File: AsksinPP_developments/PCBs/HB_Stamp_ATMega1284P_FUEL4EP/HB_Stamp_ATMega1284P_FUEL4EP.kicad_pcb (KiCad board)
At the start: 2 copper layers, 22 x 40 mm, 39 parts, among them J1 Power, J2 FTDI Debuger, J3 ISP Programmer, J4 I2C, J5 PA5/PCINT5, J6 PB3/AIN1/PCINT11, J7 PC4/PCINT20, U1 ATmega1284P-AU, U2 TPS61221DCK

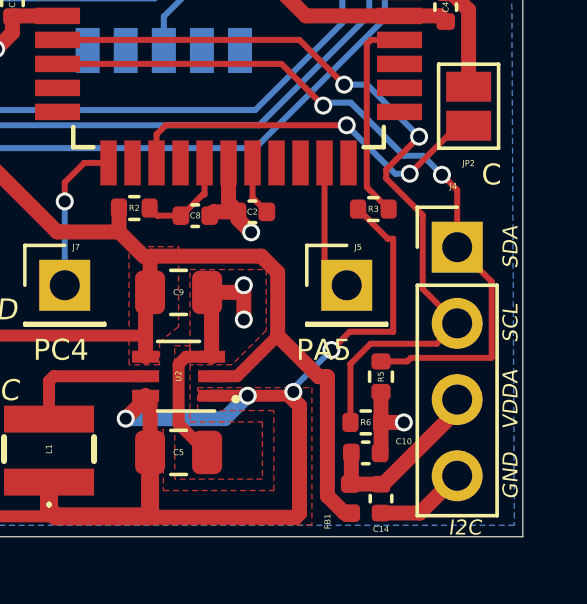
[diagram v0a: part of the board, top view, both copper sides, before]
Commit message: PCBs: HB_Stamp_ATMega1284P_FUEL4EP and I2C_Module_SHT45_BME280_small_FUEL4EP: make I2C sockets fitting each other
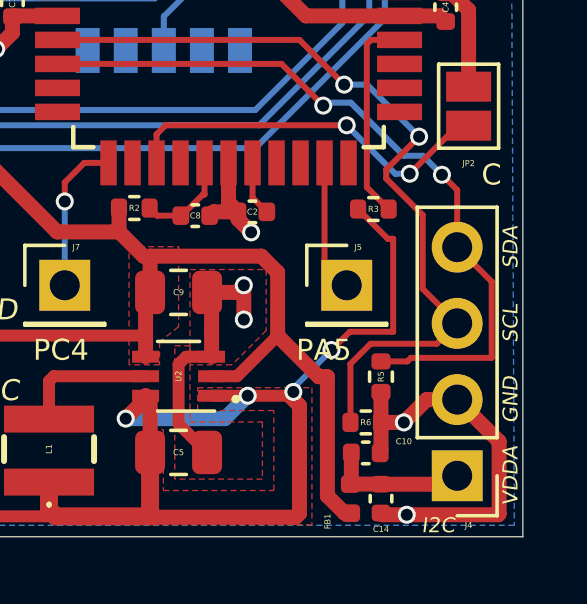
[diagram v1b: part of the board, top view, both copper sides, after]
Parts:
- moved J4 7.62 mm to (19.8, -2.03), turned to 180 degrees
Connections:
- J4 pad 1: /SDA -> /VDDA
- J4 pad 2: /SCL -> GND
- J4 pad 3: /VDDA -> /SCL
- J4 pad 4: GND -> /SDA
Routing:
- net GND: track 50.5 -> 57.9 mm, vias 12 -> 13
- net /VDDA: track 5.58 -> 4.68 mm
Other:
- board text added: "Version 1.1 - 01/2024 (KiCAD 6)"
- board text removed: "Version 1.0 - 01/2024 (KiCAD 6)"

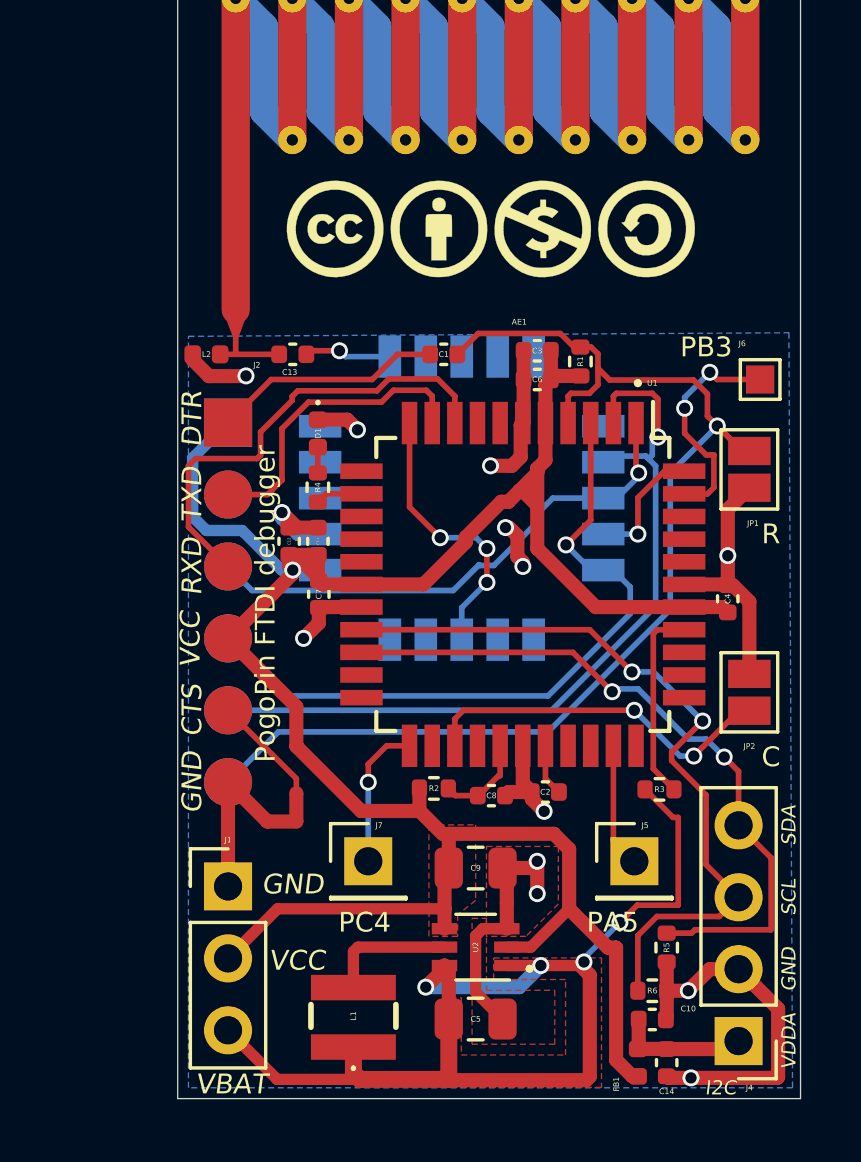
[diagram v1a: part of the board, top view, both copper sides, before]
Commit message: PCBs: updates of HB_TH_Sensor_SHT45_AllInOne_FUEL4EP and HB_Stamp_ATMega1284P_FUEL4EP see README.mds
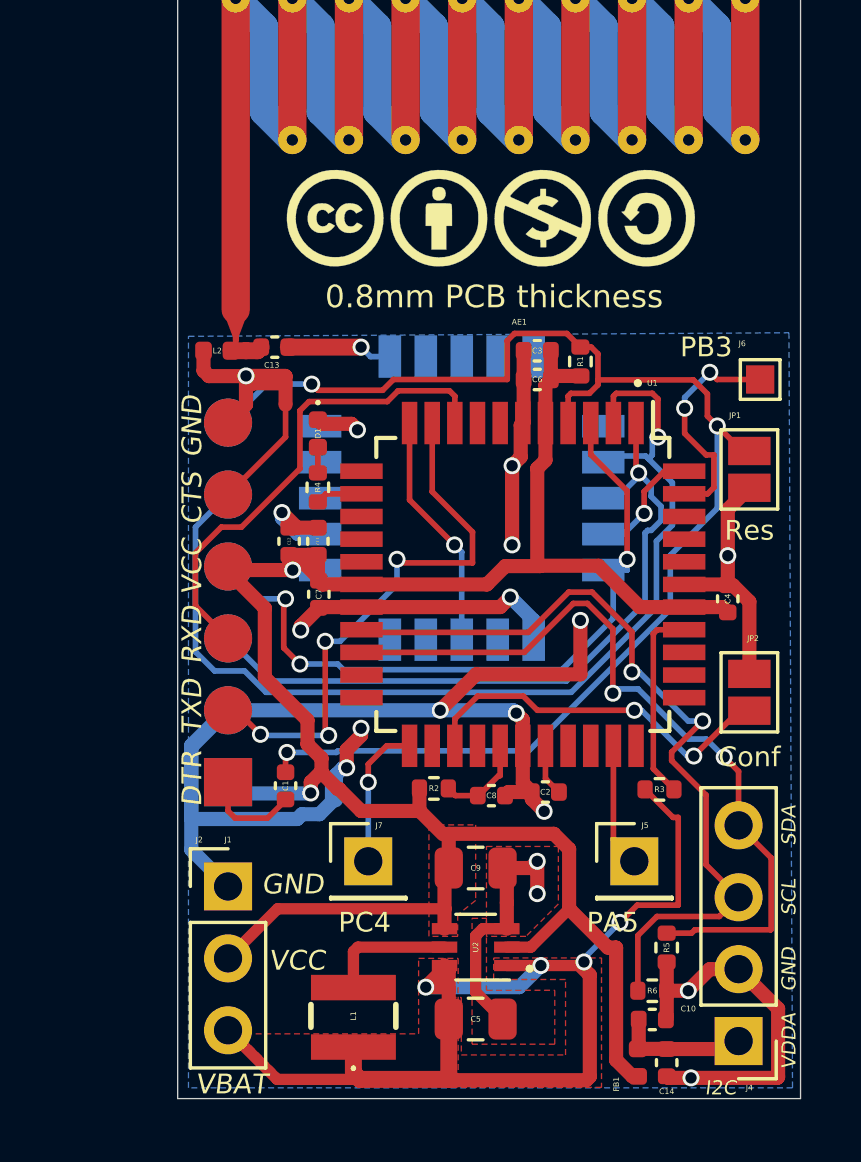
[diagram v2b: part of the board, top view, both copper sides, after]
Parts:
- moved C1 16.2 mm to (3.81, -11.0), turned to 90 degrees
- moved NT1 14.7 mm to (3.81, -25.0), turned to -90 degrees
- moved J2 12.7 mm to (1.78, -11.2), turned to 180 degrees
- moved J3 12.7 mm to (1.78, -11.2), turned to 0 degrees
- moved C13 0.68 mm to (3.43, -26.5)
- moved L2 0.40 mm to (1.40, -26.4)
- moved LOGO1 0.38 mm to (11.0, -31.1)
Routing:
- net GND: track 57.9 -> 104.4 mm, vias 13 -> 18
- net /TXD0: track 10.8 -> 19.5 mm, vias 0 -> 4
- net /MISO: track 28.4 -> 36.4 mm
- net /RSETB: track 42.2 -> 49.0 mm, vias 1 -> 3
- net /MOSI: track 18.2 -> 24.7 mm
- net VCC: track 83.8 -> 78.3 mm, vias 1 -> 2
- net /DTR: track 8.14 -> 3.42 mm
- net /SDA: track 24.9 -> 27.8 mm
- net /SCL: track 27.1 -> 29.0 mm
- net /D2: track 9.90 -> 8.42 mm, vias 3 -> 1
- net /SCK: track 24.0 -> 25.2 mm, vias 1 -> 3
- net /plusBAT: track 39.9 -> 40.7 mm
- net /ANT: track 2.91 -> 3.72 mm
- net Net-(AE1-Pad1): track 2.95 -> 2.26 mm
- net /RXD0: track 16.6 -> 17.3 mm
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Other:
- board text added: "0.8 mm PCB thickness"
- board text added: "0.8mm PCB thickness"
- board text added: "Conf"
- board text added: "Res"
- board text added: "Version 1.2 - 01/2024 (KiCAD 6)"
- board text removed: "C"
- board text removed: "PogoPin FTDI debugger"
- board text removed: "R"
- board text removed: "Version 1.1 - 01/2024 (KiCAD 6)"

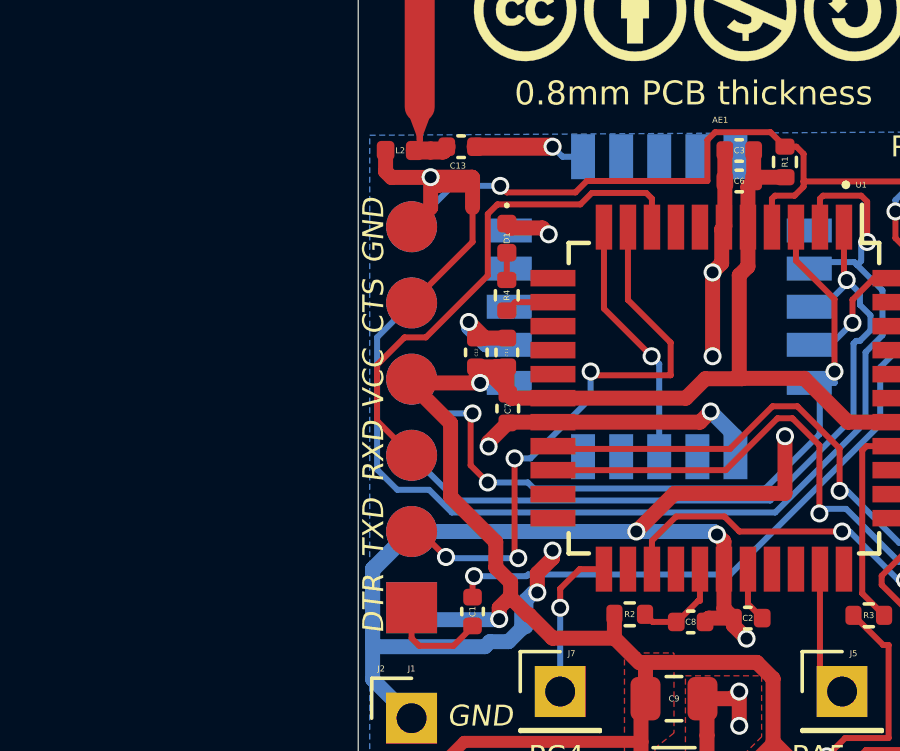
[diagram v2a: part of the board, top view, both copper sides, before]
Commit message: PCBs/HB_Stamp_ATMega1284P_FUEL4EP: added silkscreen text in PCB
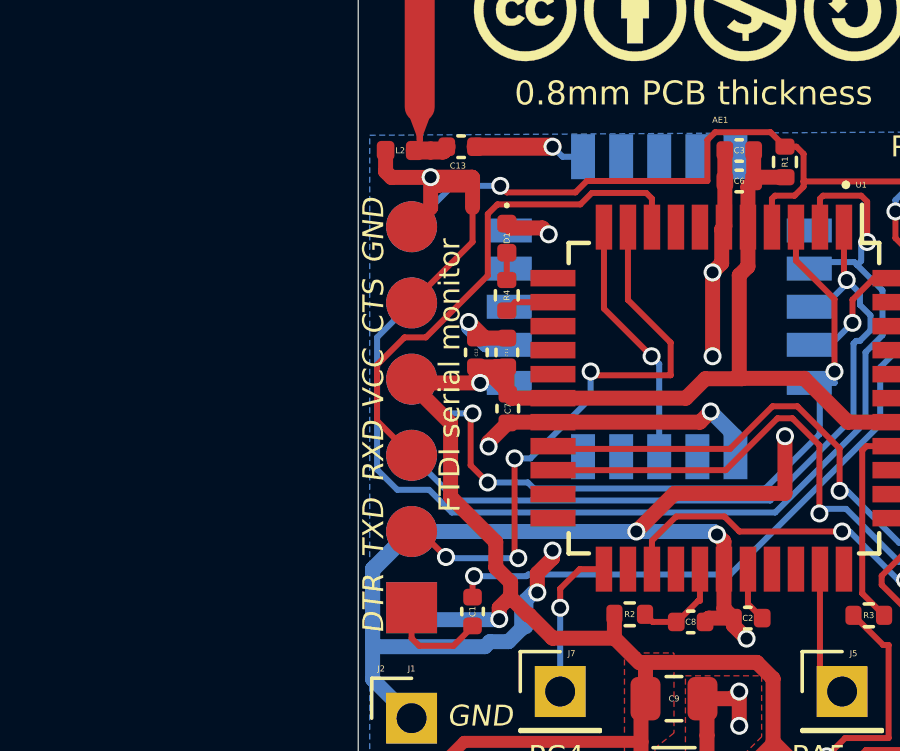
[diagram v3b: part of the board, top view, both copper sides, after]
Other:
- board text added: "FTDI serial monitor"
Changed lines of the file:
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@@
     (effects (font (size 0.7 0.7) (thickness 0.1) italic))
+  )
+  (gr_text "FTDI serial monitor" (at 3.048 -18.923 90) (layer "F.SilkS")
+    (effects (font (size 0.7 0.7) (thickness 0.15)))
   )
   (gr_text "Conf" (at 20.193 -12.065) (layer "F.SilkS")

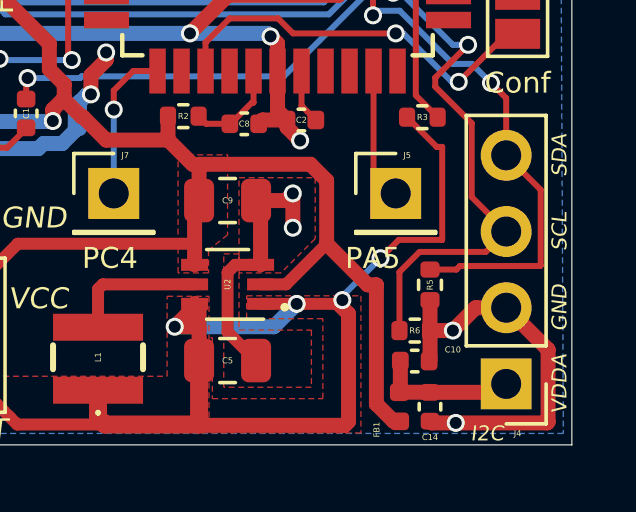
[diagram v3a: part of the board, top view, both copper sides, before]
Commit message: PCBs: fix of I2C Pull-up resistors that were wrongly tied to GND
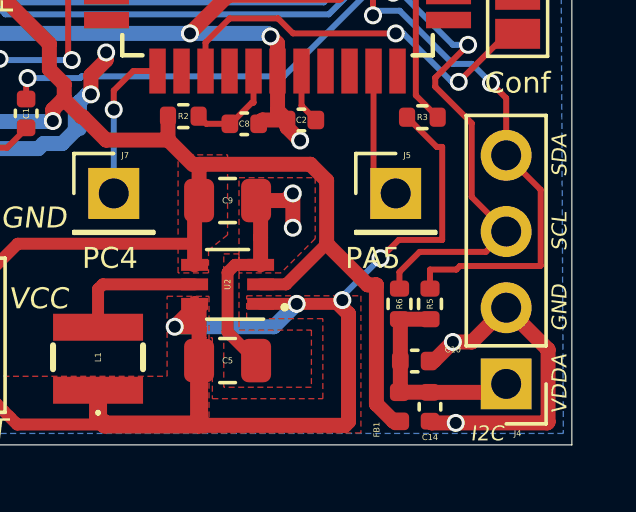
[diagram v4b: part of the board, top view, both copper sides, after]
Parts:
- R5, R6: value 4.7k -> 10k
- moved R6 1.02 mm to (16.3, -4.70), turned to 90 degrees
- moved R5 0.63 mm to (17.3, -4.70), turned to 90 degrees
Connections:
- R5 pad 1: /SDA -> /VDDA
- R5 pad 2: GND -> /SDA
- R6 pad 1: /SCL -> /VDDA
- R6 pad 2: GND -> /SCL
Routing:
- net /VDDA: track 4.28 -> 6.70 mm
- net GND: track 104.4 -> 102.8 mm
- net /SCL: track 29.0 -> 27.6 mm
- net /SDA: track 27.8 -> 28.4 mm
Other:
- board text added: "Version 1.3 - 02/2024 (KiCAD 6)"
- board text removed: "Version 1.2 - 01/2024 (KiCAD 6)"
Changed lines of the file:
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@@
   (title_block
     (title "HB_Stamp_ATMega1284P_FUEL4EP")
-    (date "2024-01-21")
-    (rev "1.2")
+    (date "2024-02-08")
+    (rev "1.3")
     (company "FUEL4EP")
   )
@@
   )
   (footprint "Resistor_SMD:R_0402_1005Metric" (layer "F.Cu")
-    (at 16.764 -3.81)
+    (at 16.256 -4.699 90)
     (descr "Resistor SMD 0402 (1005 Metric), square (rectangular) end terminal, IPC_7351 nominal, (Body size source: IPC-SM-782 page 72, https://www.pcb-3d.com/wordpress/wp-content/uploads/ipc-sm-782a_amendment_1_and_2.pdf), generated with kicad-footprint-generator")
     (tags "resistor")
-    (property "LCSC" "C25900")
+    (property "LCSC" "C25744")
     (property "Sheetfile" "HB_Stamp_ATMega1284P_FUEL4EP.kicad_sch")
     (property "Sheetname" "")
     (property "TYPE" "0402")
     (attr smd)
-    (fp_text reference "R6" (at 0 0) (layer "F.SilkS")
-      (effects (font (size 0.2 0.2) (thickness 0.15)))
-    )
-    (fp_text value "4.7k" (at 0 0.762) (layer "F.Fab")
-      (effects (font (size 0.2 0.2) (thickness 0.15)))
-    )
-    (fp_text user "${REFERENCE}" (at 0 0) (layer "F.Fab")
+    (fp_text reference "R6" (at 0 0 90) (layer "F.SilkS")
+      (effects (font (size 0.2 0.2) (thickness 0.15)))
+    )
+    (fp_text value "10k" (at 0 0.762 90) (layer "F.Fab")
+      (effects (font (size 0.2 0.2) (thickness 0.15)))
+    )
+    (fp_text user "${REFERENCE}" (at 0 0 90) (layer "F.Fab")
       (effects (font (size 0.2 0.2) (thickness 0.04)))
     )
@@
     (fp_line (start -0.525 -0.27) (end 0.525 -0.27) (layer "F.Fab") (width 0.1))
     (fp_line (start 0.525 0.27) (end -0.525 0.27) (layer "F.Fab") (width 0.1))
-    (pad "1" smd roundrect (at -0.51 0) (size 0.54 0.64) (layers "F.Cu" "F.Paste" "F.Mask") (roundrect_rratio 0.25)
+    (pad "1" smd roundrect (at -0.51 0 90) (size 0.54 0.64) (layers "F.Cu" "F.Paste" "F.Mask") (roundrect_rratio 0.25)
+      (net 7 "/VDDA") (pintype "passive"))
+    (pad "2" smd roundrect (at 0.51 0 90) (size 0.54 0.64) (layers "F.Cu" "F.Paste" "F.Mask") (roundrect_rratio 0.25)
       (net 5 "/SCL") (pintype "passive"))
-    (pad "2" smd roundrect (at 0.51 0) (size 0.54 0.64) (layers "F.Cu" "F.Paste" "F.Mask") (roundrect_rratio 0.25)
-      (net 1 "GND") (pintype "passive"))
     (model "${KICAD6_3DMODEL_DIR}/Resistor_SMD.3dshapes/R_0402_1005Metric.wrl"
       (offset (xyz 0 0 0))
@@
   )
   (footprint "Resistor_SMD:R_0402_1005Metric" (layer "F.Cu")
-    (at 17.272 -5.334 -90)
+    (at 17.272 -4.699 90)
     (descr "Resistor SMD 0402 (1005 Metric), square (rectangular) end terminal, IPC_7351 nominal, (Body size source: IPC-SM-782 page 72, https://www.pcb-3d.com/wordpress/wp-content/uploads/ipc-sm-782a_amendment_1_and_2.pdf), generated with kicad-footprint-generator")
     (tags "resistor")
-    (property "LCSC" "C25900")
+    (property "LCSC" "C25744")
     (property "Sheetfile" "HB_Stamp_ATMega1284P_FUEL4EP.kicad_sch")
     (property "Sheetname" "")
@@
       (effects (font (size 0.2 0.2) (thickness 0.15)))
     )
-    (fp_text value "4.7k" (at -0.127 0.762 90) (layer "F.Fab")
+    (fp_text value "10k" (at -0.127 0.762 90) (layer "F.Fab")
       (effects (font (size 0.2 0.2) (thickness 0.15)))
     )
@@
     (fp_line (start -0.525 -0.27) (end 0.525 -0.27) (layer "F.Fab") (width 0.1))
     (fp_line (start 0.525 0.27) (end -0.525 0.27) (layer "F.Fab") (width 0.1))
-    (pad "1" smd roundrect (at -0.51 0 270) (size 0.54 0.64) (layers "F.Cu" "F.Paste" "F.Mask") (roundrect_rratio 0.25)
+    (pad "1" smd roundrect (at -0.51 0 90) (size 0.54 0.64) (layers "F.Cu" "F.Paste" "F.Mask") (roundrect_rratio 0.25)
+      (net 7 "/VDDA") (pintype "passive"))
+    (pad "2" smd roundrect (at 0.51 0 90) (size 0.54 0.64) (layers "F.Cu" "F.Paste" "F.Mask") (roundrect_rratio 0.25)
       (net 6 "/SDA") (pintype "passive"))
-    (pad "2" smd roundrect (at 0.51 0 270) (size 0.54 0.64) (layers "F.Cu" "F.Paste" "F.Mask") (roundrect_rratio 0.25)
-      (net 1 "GND") (pintype "passive"))
     (model "${KICAD6_3DMODEL_DIR}/Resistor_SMD.3dshapes/R_0402_1005Metric.wrl"
       (offset (xyz 0 0 0))
@@
   (gr_line (start 0 -40) (end 22 -40) (layer "Edge.Cuts") (width 0.038099))
   (gr_line (start 21.336 -40.132) (end 21.336 -40.132) (layer "Edge.Cuts") (width 0.038099))
-  (gr_text "Version 1.2 - 01/2024 (KiCAD 6)\n" (at 20.701 -29.845 90) (layer "B.SilkS")
+  (gr_text "Version 1.3 - 02/2024 (KiCAD 6)\n" (at 20.701 -29.845 90) (layer "B.SilkS")
     (effects (font (size 0.7 0.7) (thickness 0.15)) (justify left mirror))
   )
@@
   (segment (start 5.098501 -23.834499) (end 6.137501 -23.834499) (width 0.5) (layer "F.Cu") (net 1))
   (segment (start 12.19 -11.145) (end 12.506 -10.829) (width 0.5) (layer "F.Cu") (net 1))
+  (segment (start 17.399 -2.794) (end 18.034 -3.429) (width 0.5) (layer "F.Cu") (net 1))
   (segment (start 11.688 -10.829) (end 11.561 -10.702) (width 0.5) (layer "F.Cu") (net 1))
   (segment (start 17.33 -0.732) (end 18.131 -0.732) (width 0.5) (layer "F.Cu") (net 1))
+  (segment (start 17.244 -2.794) (end 17.399 -2.794) (width 0.5) (layer "F.Cu") (net 1))
   (segment (start 12.22 -25.4) (end 12.22 -23.891) (width 0.5) (layer "F.Cu") (net 1))
-  (segment (start 18.796 -4.572) (end 18.034 -3.81) (width 0.5) (layer "F.Cu") (net 1))
   (segment (start 12.115 -23.786) (end 12.115 -22.661) (width 0.5) (layer "F.Cu") (net 1))
   (segment (start 19.431 -19.177) (end 19.431 -20.813) (width 0.5) (layer "F.Cu") (net 1))
-  (segment (start 17.274 -3.81) (end 17.274 -2.824) (width 0.5) (layer "F.Cu") (net 1))
   (segment (start 12.22 -23.891) (end 12.19 -23.861) (width 0.5) (layer "F.Cu") (net 1))
-  (segment (start 17.272 -4.824) (end 17.272 -3.812) (width 0.5) (layer "F.Cu") (net 1))
   (segment (start 4.345247 -16.694247) (end 4.345247 -16.549501) (width 0.5) (layer "F.Cu") (net 1))
   (segment (start 0.912 -25.713007) (end 1.106007 -25.519) (width 0.5) (layer "F.Cu") (net 1))
@@
   (segment (start 2.413 -25.527) (end 2.413 -24.511) (width 0.5) (layer "F.Cu") (net 1))
   (segment (start 5.969 -11.684) (end 5.969 -12.319) (width 0.5) (layer "F.Cu") (net 1))
-  (segment (start 19.812 -4.572) (end 18.796 -4.572) (width 0.5) (layer "F.Cu") (net 1))
+  (segment (start 18.669 -3.429) (end 18.034 -3.429) (width 0.5) (layer "F.Cu") (net 1))
   (segment (start 6.49 -17.361) (end 5.012 -17.361) (width 0.5) (layer "F.Cu") (net 1))
   (segment (start 2.675 -25.265) (end 2.413 -25.527) (width 0.5) (layer "F.Cu") (net 1))
@@
   (segment (start 3.81 -25.511) (end 2.921 -25.511) (width 0.5) (layer "F.Cu") (net 1))
   (segment (start 5.969 -12.319) (end 6.477 -12.827) (width 0.5) (layer "F.Cu") (net 1))
+  (segment (start 19.812 -4.572) (end 18.669 -3.429) (width 0.5) (layer "F.Cu") (net 1))
   (segment (start 9.271 -13.716) (end 10.541 -14.986) (width 0.5) (layer "F.Cu") (net 1))
   (segment (start 12.7 -8.382) (end 12.7 -7.239) (width 0.5) (layer "F.Cu") (net 1))
@@
   (segment (start 12.506 -10.584073) (end 12.943781 -10.146292) (width 0.5) (layer "F.Cu") (net 1))
   (segment (start 11.475 -2.81) (end 10.525 -3.76) (width 0.4) (layer "F.Cu") (net 1))
-  (segment (start 17.274 -3.81) (end 18.034 -3.81) (width 0.5) (layer "F.Cu") (net 1))
   (segment (start 6.49 -17.361) (end 11.392 -17.361) (width 0.5) (layer "F.Cu") (net 1))
   (segment (start 6.137501 -23.834499) (end 6.35 -23.622) (width 0.5) (layer "F.Cu") (net 1))
@@
   (via (at 11.7475 -17.7165) (size 0.6) (drill 0.4) (layers "F.Cu" "B.Cu") (net 1))
   (via (at 2.413 -25.527) (size 0.6) (drill 0.4) (layers "F.Cu" "B.Cu") (net 1))
-  (via (at 18.034 -3.81) (size 0.6) (drill 0.4) (layers "F.Cu" "B.Cu") (net 1))
+  (via (at 18.034 -3.429) (size 0.6) (drill 0.4) (layers "F.Cu" "B.Cu") (net 1))
   (via (at 9.271 -13.716) (size 0.6) (drill 0.4) (layers "F.Cu" "B.Cu") (net 1))
   (via (at 6.35 -23.622) (size 0.6) (drill 0.4) (layers "F.Cu" "B.Cu") (net 1))
@@
   (segment (start 10.033 -19.304) (end 9.779 -19.558) (width 0.2) (layer "B.Cu") (net 4))
   (segment (start 10.033 -16.209) (end 10.033 -19.304) (width 0.2) (layer "B.Cu") (net 4))
-  (segment (start 16.254 -5.761183) (end 16.254 -3.81) (width 0.2) (layer "F.Cu") (net 5))
   (segment (start 18.662 -8.262) (end 18.662 -10.723183) (width 0.2) (layer "F.Cu") (net 5))
   (segment (start 13.810199 -17.890001) (end 14.637801 -17.890001) (width 0.2) (layer "F.Cu") (net 5))
   (segment (start 12.388697 -16.468499) (end 13.810199 -17.890001) (width 0.2) (layer "F.Cu") (net 5))
+  (segment (start 16.254 -5.211) (end 16.256 -5.209) (width 0.2) (layer "F.Cu") (net 5))
+  (segment (start 16.254 -5.761183) (end 16.254 -5.211) (width 0.2) (layer "F.Cu") (net 5))
   (segment (start 16.044911 -16.482891) (end 16.044911 -15.070089) (width 0.2) (layer "F.Cu") (net 5))
   (segment (start 16.925316 -6.432499) (end 16.254 -5.761183) (width 0.2) (layer "F.Cu") (net 5))
@@
   (segment (start 18.26796 -5.962) (end 18.14996 -5.844) (width 0.2) (layer "F.Cu") (net 6))
   (segment (start 20.948 -5.962) (end 18.26796 -5.962) (width 0.2) (layer "F.Cu") (net 6))
+  (segment (start 17.272 -5.844) (end 17.272 -5.209) (width 0.2) (layer "F.Cu") (net 6))
   (segment (start 20.962 -8.502) (end 20.962 -5.976) (width 0.2) (layer "F.Cu") (net 6))
   (segment (start 19.812 -11.557) (end 19.304 -12.065) (width 0.2) (layer "F.Cu") (net 6))
@@
   (segment (start 16.263411 -14.470589) (end 15.524219 -14.470589) (width 0.2) (layer "B.Cu") (net 6))
   (segment (start 19.304 -12.065) (end 18.669 -12.7) (width 0.2) (layer "B.Cu") (net 6))
+  (segment (start 16.284 -2.794) (end 16.284 -4.161) (width 0.5) (layer "F.Cu") (net 7))
+  (segment (start 17.272 -4.189) (end 16.256 -4.189) (width 0.5) (layer "F.Cu") (net 7))
+  (segment (start 16.284 -4.161) (end 16.256 -4.189) (width 0.5) (layer "F.Cu") (net 7))
   (segment (start 17.272 -1.75) (end 19.53 -1.75) (width 0.5) (layer "F.Cu") (net 7))
   (segment (start 16.256 -1.755) (end 17.267 -1.755) (width 0.5) (layer "F.Cu") (net 7))
